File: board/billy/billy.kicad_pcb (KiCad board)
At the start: 2 copper layers, 70 x 50 mm, 65 parts, among them J1 Screw_Terminal_01x02, J10 Screw_Terminal_01x02, J11 Screw_Terminal_01x02, J2 Conn_01x06, J3 Screw_Terminal_01x02, J4 Screw_Terminal_01x02, J5 USB_C_Receptacle_USB2.0_16P, J6 Screw_Terminal_01x02, J8 Screw_Terminal_01x03, J9 Screw_Terminal_01x02, Q1 AO3400A, Q2 AO3400A, Q3 AO3400A, SW1 TS-1088-AR02016, U1 ESP32-S3-WROOM-1, U2 DRV8833PWP, U3 MAX98357A, U4 DRV8833PWP

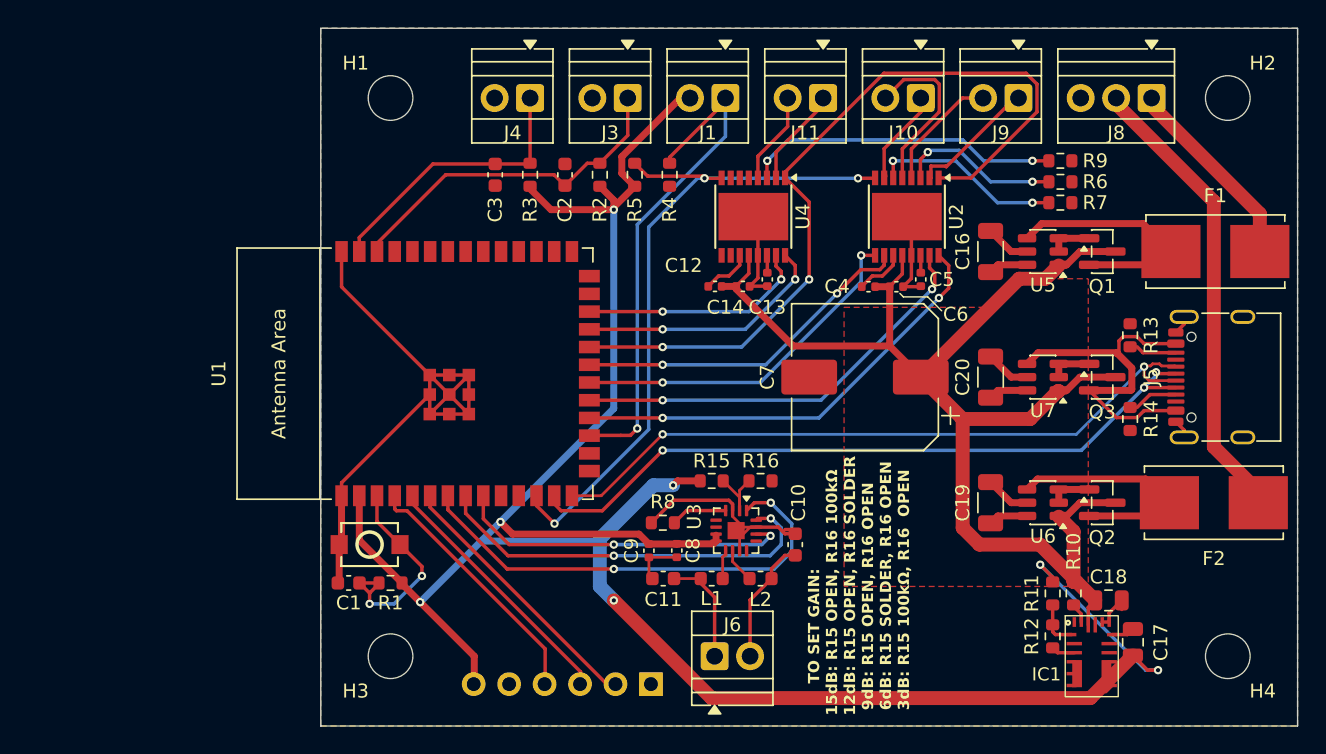
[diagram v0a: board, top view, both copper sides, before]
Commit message: Add gated status LED (WS2812, low-side FET VDD switch) to schematic/board and firmware
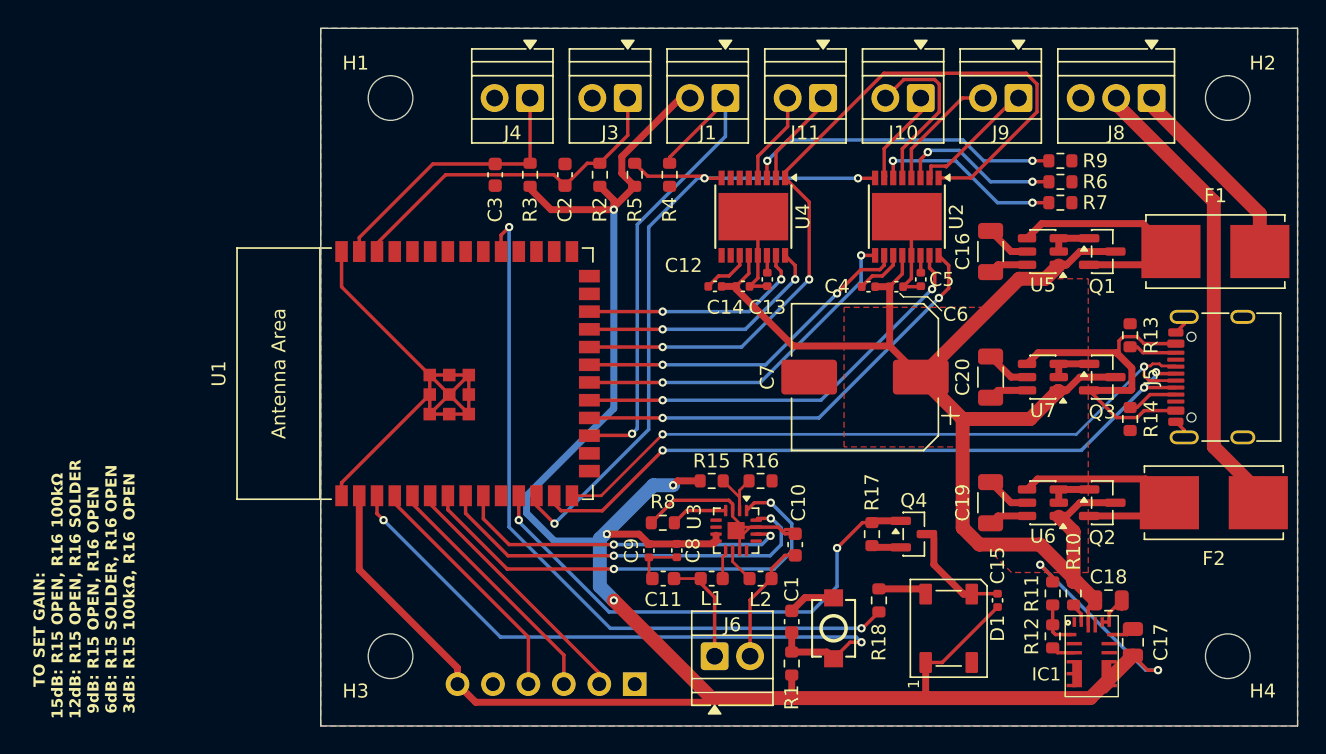
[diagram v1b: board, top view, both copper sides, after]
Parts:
- added C15: 100n, Capacitor_SMD:C_0402_1005Metric, F.Cu at (198.5, 91.0)
- added D1: WS2812B, LED_SMD:LED_WS2812B_PLCC4_5.0x5.0mm_P3.2mm, F.Cu at (195.0, 93.0)
- added Q4: AO3400A, Package_TO_SOT_SMD:SOT-23, F.Cu at (192.5, 86.2)
- added R17: 10k, Resistor_SMD:R_0603_1608Metric, F.Cu at (189.5, 86.2)
- added R18: 470, Resistor_SMD:R_0603_1608Metric, F.Cu at (190.0, 91.0)
- C12, C4: value 0.01u -> 10n
- C9: value 0.1u -> 100n
- moved SW1 33.8 mm to (186.8, 93.0), turned to -90 degrees
- moved C1 31.9 mm to (183.8, 92.5), turned to 90 degrees
- moved R1 29.3 mm to (183.8, 95.5), turned to 90 degrees
- moved J2 1.16 mm to (172.5, 97.0)
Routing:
- net GPIO38: track 0.00 -> 53.5 mm, vias 0 -> 2
- net GPIO18: track 0.00 -> 36.3 mm, vias 0 -> 2
- net EN: track 16.1 -> 46.9 mm
- net +3.3V: track 170.8 -> 180.4 mm, vias 7 -> 6
- net Net-(D1-VSS): track 0.00 -> 7.39 mm
- net Net-(D1-DIN): track 0.00 -> 3.51 mm
- net GND: track 89.5 -> 88.3 mm
- net GPIO4: track 18.4 -> 17.5 mm
- net GPIO6: track 19.4 -> 18.5 mm

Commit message: Complete board layout, assign LCSC part numbers, verify footprints; passes DRC
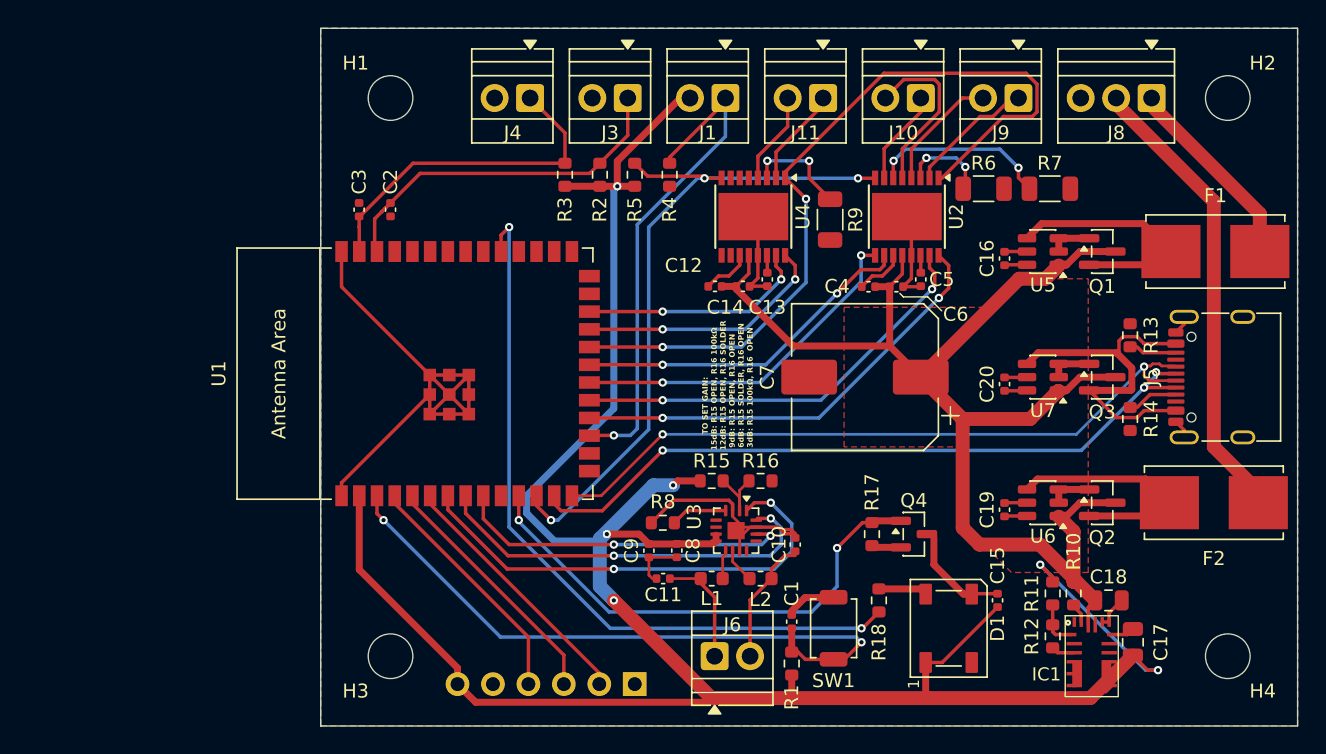
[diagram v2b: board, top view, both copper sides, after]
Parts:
- C1, C10, C11, C2, C3: footprint Capacitor_SMD:C_0603_1608Metric -> Capacitor_SMD:C_0402_1005Metric
- C16, C19, C20: footprint Capacitor_SMD:C_1206_3216Metric -> Capacitor_SMD:C_0402_1005Metric
- L1, L2: value 0.15 -> 50m
- R6, R7, R9: footprint Resistor_SMD:R_0603_1608Metric -> Resistor_SMD:R_1206_3216Metric
- SW1: footprint billy:SW-SMD_L3.9-W3.0-P4.45 -> Button_Switch_SMD:SW_SPST_TS-1088-xR020
- U2, U4: value DRV8833PWP -> DRV8833PWPR
- moved R9 17.0 mm to (186.5, 63.7), turned to -90 degrees
- moved C2 12.7 mm to (155.0, 63.0), turned to -90 degrees
- moved C3 10.1 mm to (152.8, 63.0), turned to 90 degrees
- moved R6 5.53 mm to (197.5, 61.5)
- moved R3 2.50 mm to (167.5, 60.5)
- moved R7 1.25 mm to (202.2, 61.5)
- moved C16 1.12 mm to (199.0, 66.5)
- moved C19 1.12 mm to (199.0, 84.5)
- moved C20 1.12 mm to (199.0, 75.5)
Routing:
- net Net-(U4-AISEN): track 22.7 -> 7.61 mm
- net Net-(U2-AISEN): track 11.7 -> 6.29 mm
- net +3.3V: track 180.4 -> 175.0 mm
- net GPIO1: track 20.1 -> 24.6 mm
- net GND: track 88.3 -> 86.0 mm
- net Net-(U7-V_CAPH): track 3.22 -> 1.59 mm
- net Net-(U6-V_CAPH): track 3.22 -> 1.59 mm
- net Net-(U5-V_CAPH): track 3.22 -> 1.59 mm
- net Net-(Q1-S): track 17.8 -> 16.5 mm
- net Net-(Q2-S): track 17.4 -> 16.0 mm
- net Net-(U7-V_CAPL): track 2.83 -> 1.58 mm
- net Net-(U6-V_CAPL): track 2.83 -> 1.58 mm
- net Net-(U5-V_CAPL): track 2.83 -> 1.58 mm
- net Net-(J8-Pin_2): track 33.2 -> 32.0 mm
- net Net-(U2-BISEN): track 13.7 -> 12.9 mm
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
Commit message: Fix some minor ERC and DRC checks
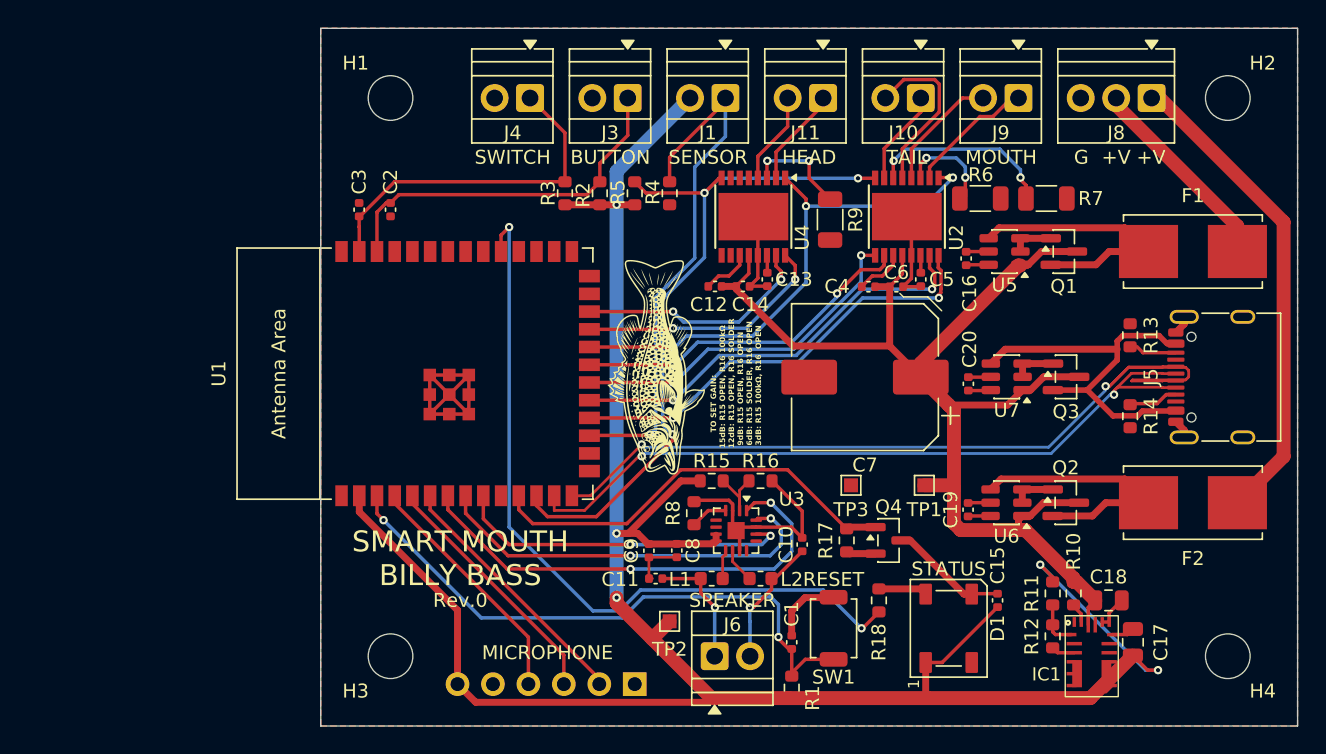
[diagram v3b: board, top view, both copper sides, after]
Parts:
- added ?: LOGO, LOGO, F.Cu at (174.0, 74.3)
- added TP1: TestPoint, TestPoint:TestPoint_Pad_1.0x1.0mm, F.Cu at (193.2, 82.8)
- added TP2: TestPoint, TestPoint:TestPoint_Pad_1.0x1.0mm, F.Cu at (175.0, 92.5)
- added TP3: TestPoint, TestPoint:TestPoint_Pad_1.0x1.0mm, F.Cu at (188.0, 82.8)
- moved C16 2.75 mm to (196.2, 66.5)
- moved Q1 2.75 mm to (203.2, 66.0)
- moved U5 2.75 mm to (199.0, 66.0)
- moved C19 2.61 mm to (196.4, 84.5)
- moved Q2 2.61 mm to (203.4, 84.0)
- moved U6 2.61 mm to (199.1, 84.0)
- moved C20 2.59 mm to (196.4, 75.5)
- moved Q3 2.59 mm to (203.4, 75.0)
- moved U7 2.59 mm to (199.2, 75.0)
- moved R8 2.34 mm to (176.8, 84.8), turned to 90 degrees
- moved Q4 1.87 mm to (190.7, 86.7)
- moved R17 1.87 mm to (187.7, 86.7)
- moved R1 1.72 mm to (183.8, 97.2)
- moved F1 1.61 mm to (212.5, 66.0)
- moved F2 1.50 mm to (212.5, 84.0)
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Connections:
- net /H_MOTOR1 renamed Net-(J11-Pin_1)
- net /H_MOTOR2 renamed Net-(J11-Pin_2)
- net /M_MOTOR1 renamed Net-(J9-Pin_1)
- net /M_MOTOR2 renamed Net-(J9-Pin_2)
- net /T_MOTOR1 renamed Net-(J10-Pin_1)
- net /T_MOTOR2 renamed Net-(J10-Pin_2)
- net D+ renamed U_P
- net D- renamed U_N
- F1 pad 1: Net-(J8-Pin_1) -> Net-(J8-Pin_2)
- F2 pad 1: Net-(J8-Pin_2) -> Net-(J8-Pin_1)
- U1 pad 10: GPIO17 -> unconnected-(U1-GPIO17/U1TXD/ADC2_CH6-Pad10)
- U1 pad 15: GPIO3 -> unconnected-(U1-GPIO3/TOUCH3/ADC1_CH2-Pad15)
- U1 pad 16: GPIO46 -> unconnected-(U1-GPIO46-Pad16)
- U1 pad 25: GPIO48 -> unconnected-(U1-GPIO48/SPICLK_N/SUBSPICLK_N_DIFF-Pad25)
- U1 pad 26: GPIO45 -> unconnected-(U1-GPIO45-Pad26)
- U1 pad 27: GPIO0 -> unconnected-(U1-GPIO0/BOOT-Pad27)
- U1 pad 28: GPIO35 -> unconnected-(U1-SPIIO6/GPIO35/FSPID/SUBSPID-Pad28)
- U1 pad 29: GPIO36 -> unconnected-(U1-SPIIO7/GPIO36/FSPICLK/SUBSPICLK-Pad29)
- U1 pad 30: GPIO37 -> unconnected-(U1-SPIDQS/GPIO37/FSPIQ/SUBSPIQ-Pad30)
- U1 pad 32: GPIO39 -> unconnected-(U1-MTCK/GPIO39/CLK_OUT3/SUBSPICS1-Pad32)
- U1 pad 33: GPIO40 -> unconnected-(U1-MTDO/GPIO40/CLK_OUT2-Pad33)
- U1 pad 34: GPIO41 -> unconnected-(U1-MTDI/GPIO41/CLK_OUT1-Pad34)
- U1 pad 35: GPIO42 -> unconnected-(U1-MTMS/GPIO42-Pad35)
- U1 pad 36: GPIO44 -> unconnected-(U1-U0RXD/GPIO44/CLK_OUT2-Pad36)
- U1 pad 37: GPIO43 -> unconnected-(U1-U0TXD/GPIO43/CLK_OUT1-Pad37)
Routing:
- net Net-(J8-Pin_1): track 14.2 -> 34.6 mm
- net GPIO14: track 58.3 -> 37.9 mm, vias 2 -> 3
- net GND: track 86.0 -> 66.1 mm
- net Net-(J8-Pin_2): track 32.0 -> 14.6 mm
- net +3.3V: track 175.0 -> 162.6 mm, vias 6 -> 5
- net U_P: track 50.4 -> 61.6 mm
- net GPIO18: track 36.0 -> 30.2 mm, vias 2 -> 0
- net Vdrive: track 92.7 -> 87.0 mm
- net EN: track 46.9 -> 42.9 mm
- net Net-(Q2-S): track 16.0 -> 19.6 mm
- net Net-(Q1-S): track 16.5 -> 19.9 mm
- net U_N: track 51.3 -> 54.4 mm, vias 3 -> 2
- net Net-(Q3-S): track 25.4 -> 28.2 mm
- net GPIO9: track 36.0 -> 38.1 mm
- net Net-(U3-~{SD_MODE}): track 4.04 -> 2.68 mm
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- removed copper zone on F.Cu, net Vdrive
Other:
- board text added: "+V"
- board text added: "BUTTON"
- board text added: "G"
- board text added: "HEAD"
- board text added: "MICROPHONE"
- board text added: "MOUTH"
- board text added: "RESET"
- board text added: "Rev.0"
- board text added: "SENSOR"
- board text added: "SMART MOUTH BILLY BASS"
- board text added: "SPEAKER"
- board text added: "STATUS"
- board text added: "SWITCH"
- board text added: "TAIL"

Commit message: Switched to Micro-USB 2.0
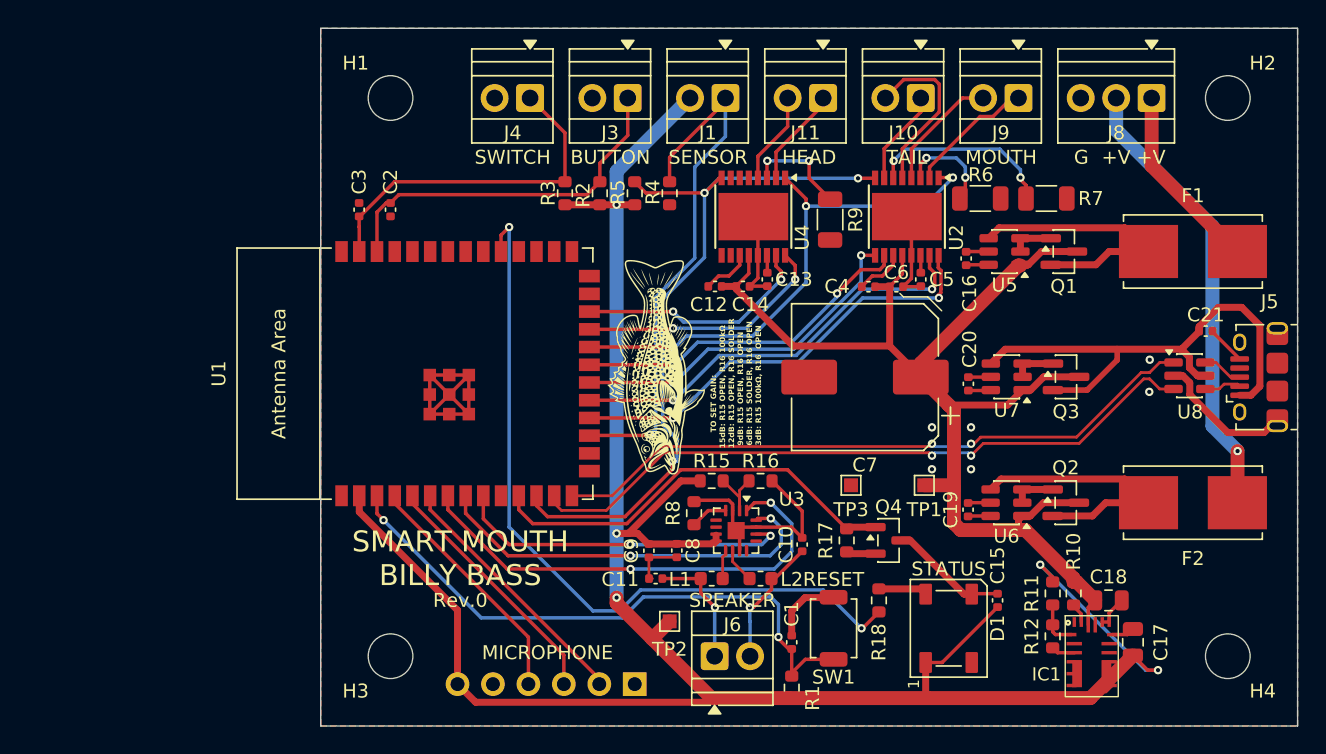
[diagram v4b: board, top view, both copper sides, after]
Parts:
- removed R13, R14: 5.1k, Resistor_SMD:R_0603_1608Metric
- added C21: 100n, Capacitor_SMD:C_0402_1005Metric, F.Cu at (213.4, 71.7)
- added U8: USBLC6-2SC6, Package_TO_SOT_SMD:SOT-23-6, F.Cu at (212.2, 74.9)
- J5: value USB_C_Receptacle_USB2.0_16P -> USB_B_Micro; footprint Connector_USB:USB_C_Receptacle_G-Switch_GT-USB-7010ASV -> Connector_USB:USB_Micro-B_Amphenol_10118194-0001LF_Horizontal
- moved J5 2.25 mm to (217.2, 75.0)
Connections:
- F1 pad 1: Net-(J8-Pin_2) -> Net-(J8-Pin_1)
- F2 pad 1: Net-(J8-Pin_1) -> Net-(J8-Pin_2)
- Q3 pad 2: Net-(Q3-S) -> Net-(J5-VBUS)
- U7 pad 4: Net-(Q3-S) -> Net-(J5-VBUS)
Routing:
- net Net-(J5-VBUS): track 0.00 -> 36.9 mm
- net Net-(Q3-S): track 28.2 -> 0.00 mm
- net Net-(J8-Pin_1): track 34.6 -> 13.5 mm
- net Net-(J8-Pin_2): track 14.6 -> 32.6 mm, vias 0 -> 1
- net U_P: track 61.6 -> 47.2 mm
- net GND: track 66.1 -> 76.1 mm, vias 0 -> 6
- net U_N: track 54.4 -> 49.1 mm
- net Net-(J5-CC1): track 3.47 -> 0.00 mm
- net Net-(J5-CC2): track 2.93 -> 0.00 mm
- net Net-(J5-D+): track 0.00 -> 2.90 mm
- net Net-(J5-D-): track 0.00 -> 2.67 mm
- net GPIO8: track 51.9 -> 53.6 mm

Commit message: Add fiducials and thermal vias, clean up USB diff pair routing
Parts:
- added FID1: Fiducial_1mm_Mask2mm, Fiducial:Fiducial_1mm_Mask2mm, F.Cu at (158.6, 58.7)
- added FID2: Fiducial_1mm_Mask2mm, Fiducial:Fiducial_1mm_Mask2mm, F.Cu at (214.6, 60.2)
- added FID3: Fiducial_1mm_Mask2mm, Fiducial:Fiducial_1mm_Mask2mm, F.Cu at (210.2, 90.6)
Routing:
- net GND: vias 6 -> 30

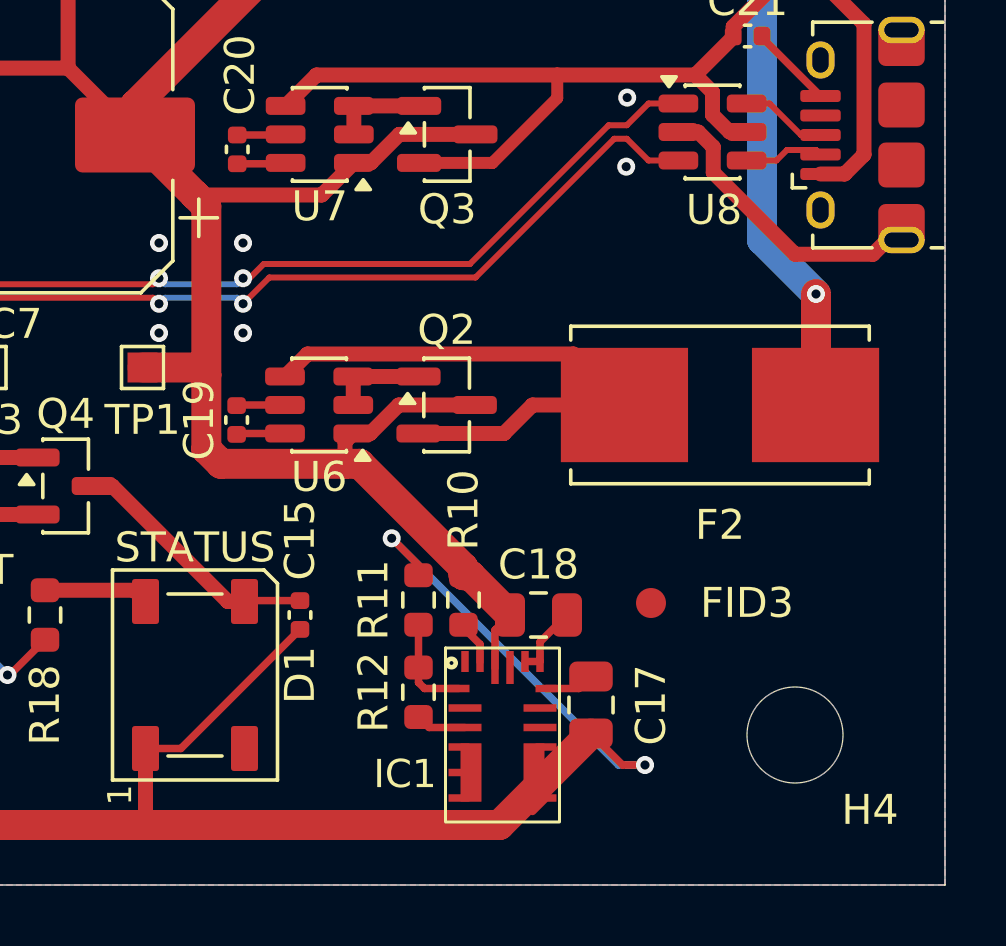
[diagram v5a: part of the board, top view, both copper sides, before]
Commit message: Populate MPM3610 AAM resistor (R13, 82k) to enable light-load power-save mode
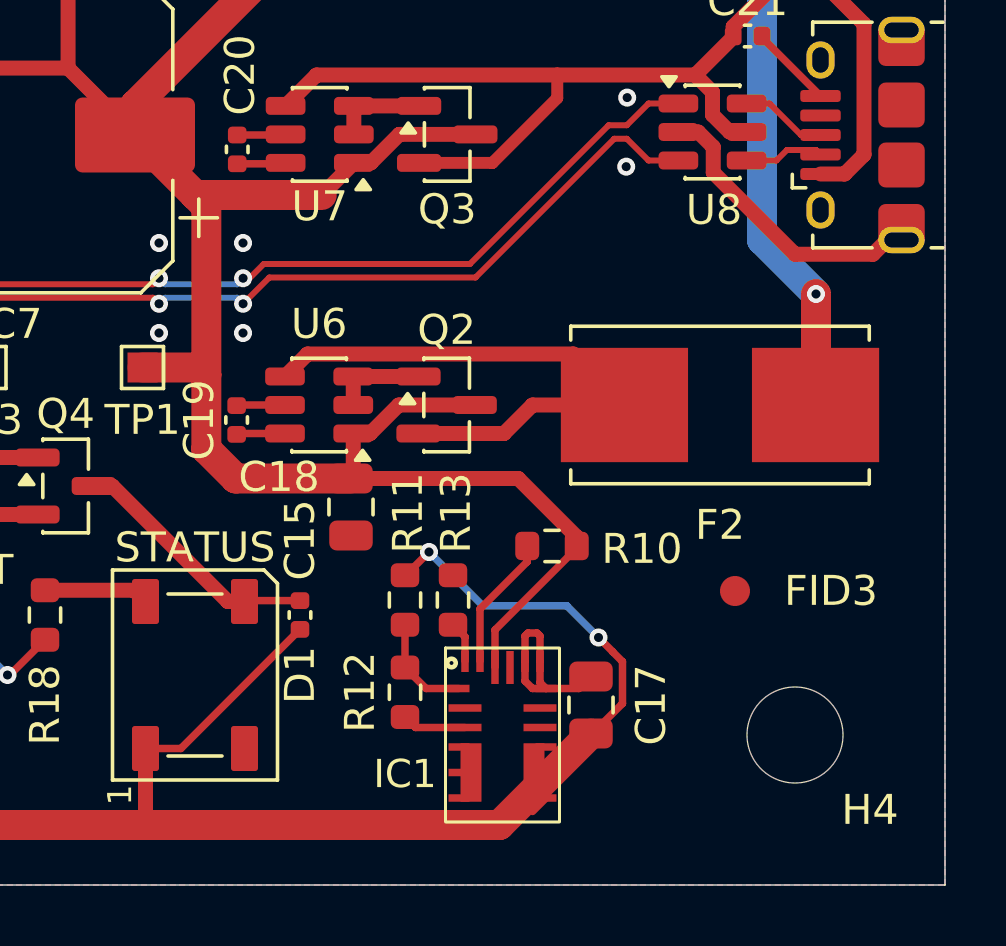
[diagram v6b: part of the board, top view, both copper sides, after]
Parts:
- added R13: 82k, Resistor_SMD:R_0603_1608Metric, F.Cu at (203.6, 90.5)
- moved C18 7.21 mm to (200.2, 87.4), turned to -90 degrees
- moved R10 3.46 mm to (206.9, 88.7), turned to 0 degrees
- moved FID3 2.83 mm to (213.0, 90.2)
- moved R11 0.45 mm to (202.0, 90.5)
- moved R12 0.45 mm to (202.0, 93.6)
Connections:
- IC1 pad 18: unconnected-(IC1-AAM-Pad18) -> Net-(IC1-AAM)
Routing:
- net Vdrive: track 87.0 -> 91.7 mm
- net +3.3V: track 162.6 -> 159.0 mm
- net Net-(IC1-EN): track 1.35 -> 4.50 mm
- net GND: track 76.1 -> 78.9 mm
- net Net-(IC1-AAM): track 0.00 -> 1.39 mm
